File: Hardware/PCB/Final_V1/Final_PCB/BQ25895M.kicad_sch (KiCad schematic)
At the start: 17 parts, among them IC1 BQ25895MRTWT

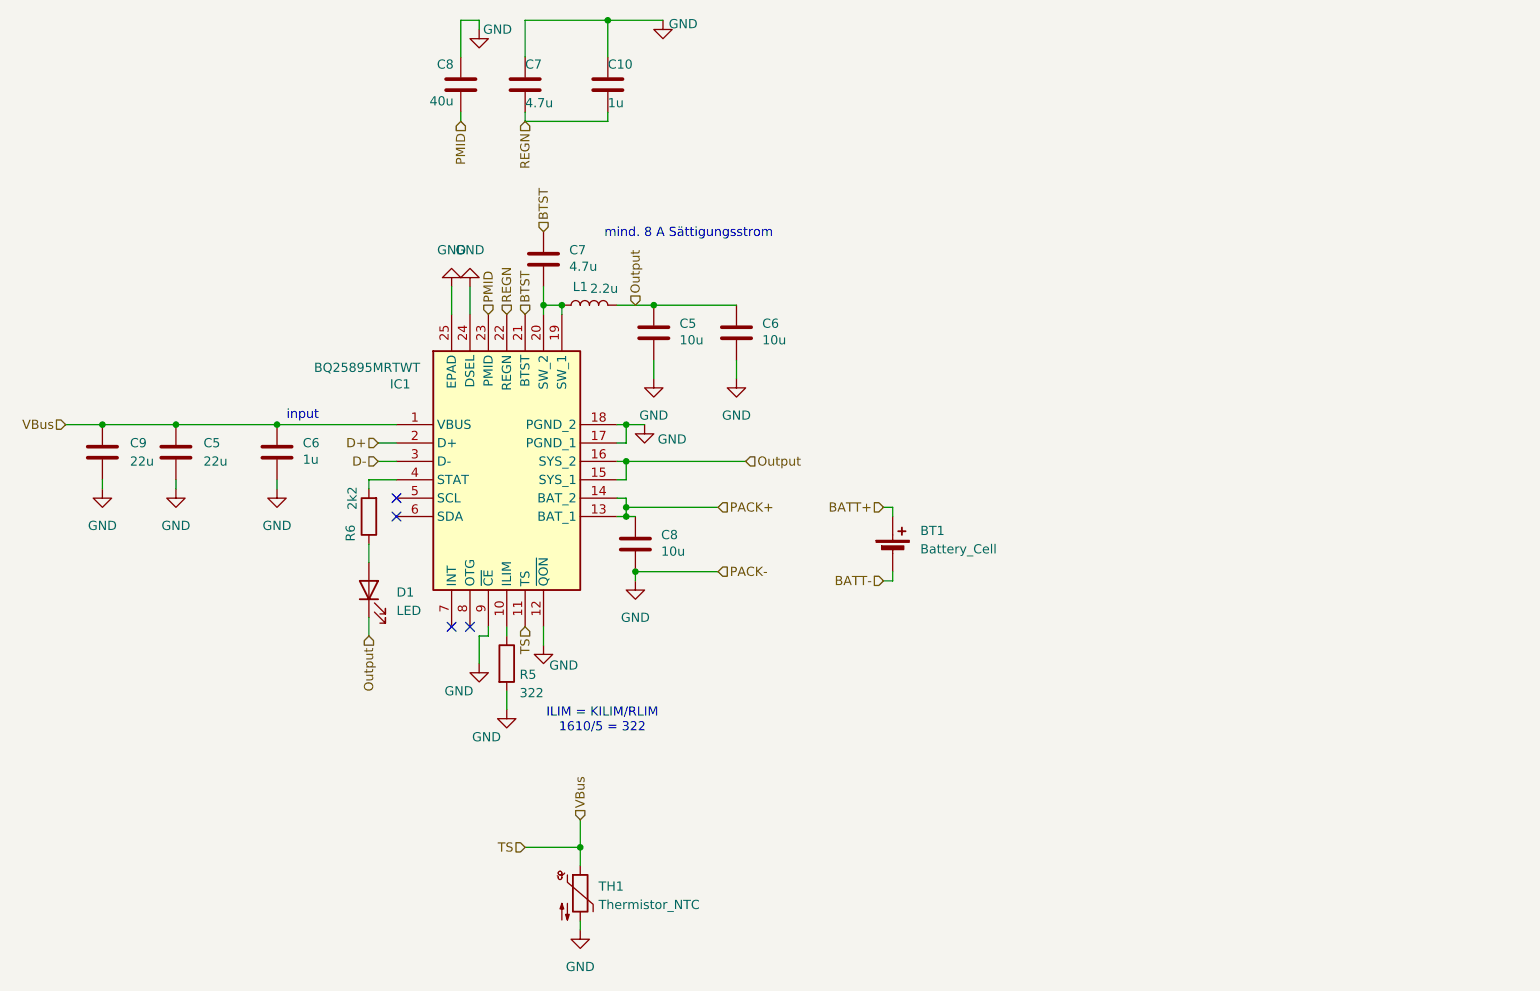
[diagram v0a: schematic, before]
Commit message: added Voltage regulator to get constant 3.3V Voltage and fixed some issues
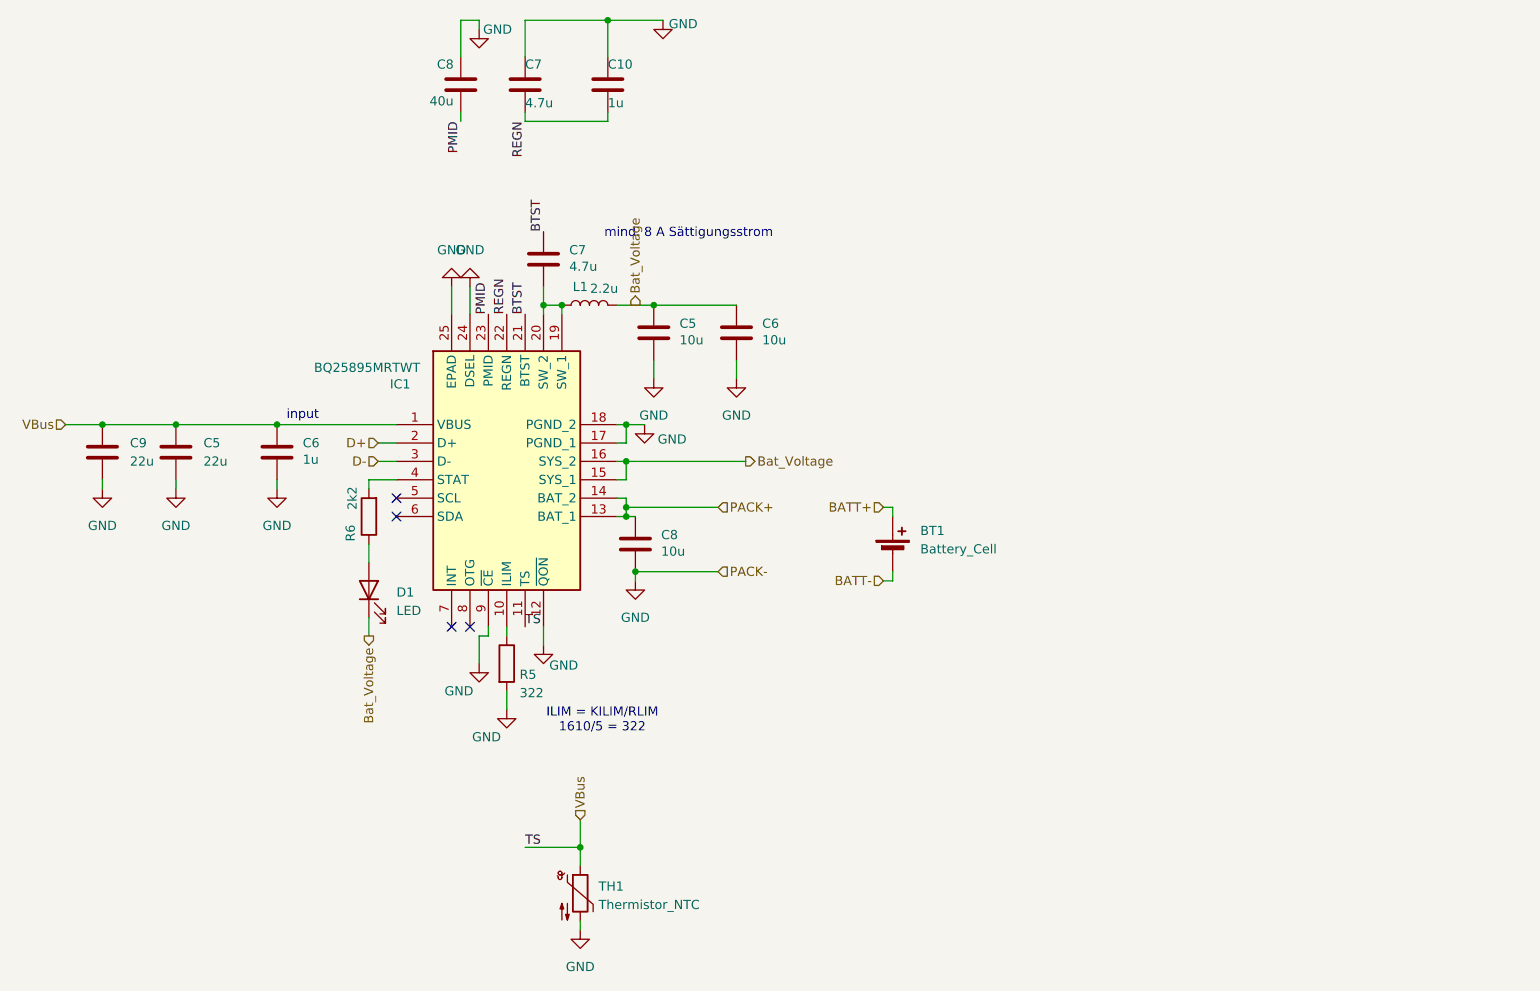
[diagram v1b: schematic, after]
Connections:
- net Output renamed Bat_Voltage
- net TS renamed VBus
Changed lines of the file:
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@@
+		)
+	)
+	(label "BTST"
+		(at 133.35 69.85 90)
+		(effects
+			(font
+				(size 1.27 1.27)
+			)
+			(justify left bottom)
+		)
+	)
+	(label "PMID"
+		(at 128.27 69.85 90)
+		(effects
+			(font
+				(size 1.27 1.27)
+			)
+			(justify left bottom)
+		)
+	)
+	(label "REGN"
+		(at 133.35 43.18 270)
+		(effects
+			(font
+				(size 1.27 1.27)
+			)
+			(justify right bottom)
+		)
+	)
+	(label "REGN"
+		(at 130.81 69.85 90)
+		(effects
+			(font
+				(size 1.27 1.27)
+			)
+			(justify left bottom)
+		)
+	)
+	(label "TS"
+		(at 133.35 113.03 0)
+		(effects
+			(font
+				(size 1.27 1.27)
+			)
+			(justify left bottom)
+		)
+	)
+	(label "BTST"
+		(at 135.89 58.42 90)
+		(effects
+			(font
+				(size 1.27 1.27)
+			)
+			(justify left bottom)
+		)
+	)
+	(label "TS"
+		(at 133.35 143.51 0)
+		(effects
+			(font
+				(size 1.27 1.27)
+			)
+			(justify left bottom)
+		)
+	)
+	(label "PMID"
+		(at 124.46 43.18 270)
+		(effects
+			(font
+				(size 1.27 1.27)
+			)
+			(justify right bottom)
 		)
 	)
@@
 		)
 	)
-	(hierarchical_label "Output"
-		(shape input)
+	(hierarchical_label "Bat_Voltage"
+		(shape output)
 		(at 163.83 90.17 0)
 		(effects
@@
 		)
 	)
-	(hierarchical_label "Output"
-		(shape input)
+	(hierarchical_label "Bat_Voltage"
+		(shape output)
 		(at 111.76 114.3 270)
 		(effects
@@
 		)
 	)
-	(hierarchical_label "PMID"
-		(shape input)
-		(at 128.27 69.85 90)
-		(effects
-			(font
-				(size 1.27 1.27)
-			)
-			(justify left)
-		)
-	)
 	(hierarchical_label "BATT+"
 		(shape input)
@@
 		)
 	)
-	(hierarchical_label "REGN"
-		(shape input)
-		(at 130.81 69.85 90)
-		(effects
-			(font
-				(size 1.27 1.27)
-			)
-			(justify left)
-		)
-	)
-	(hierarchical_label "Output"
-		(shape input)
+	(hierarchical_label "Bat_Voltage"
+		(shape output)
 		(at 148.59 68.58 90)
 		(effects
@@
 		)
 	)
-	(hierarchical_label "BTST"
-		(shape input)
-		(at 135.89 58.42 90)
-		(effects
-			(font
-				(size 1.27 1.27)
-			)
-			(justify left)
-		)
-	)
 	(hierarchical_label "PACK-"
 		(shape input)
@@
 		)
 	)
-	(hierarchical_label "PMID"
-		(shape input)
-		(at 124.46 43.18 270)
-		(effects
-			(font
-				(size 1.27 1.27)
-			)
-			(justify right)
-		)
-	)
 	(hierarchical_label "PACK+"
 		(shape input)
@@
 		(effects
 			(font
-				(size 1.27 1.27)
-			)
-			(justify left)
-		)
-	)
-	(hierarchical_label "TS"
-		(shape input)
-		(at 133.35 113.03 270)
-		(effects
-			(font
-				(size 1.27 1.27)
-			)
-			(justify right)
-		)
-	)
-	(hierarchical_label "TS"
-		(shape input)
-		(at 133.35 143.51 180)
-		(effects
-			(font
-				(size 1.27 1.27)
-			)
-			(justify right)
-		)
-	)
-	(hierarchical_label "REGN"
-		(shape input)
-		(at 133.35 43.18 270)
-		(effects
-			(font
-				(size 1.27 1.27)
-			)
-			(justify right)
-		)
-	)
-	(hierarchical_label "BTST"
-		(shape input)
-		(at 133.35 69.85 90)
-		(effects
-			(font

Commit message: fixing xhematics
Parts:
- renumbered C7 to C13, C5 to C15, C6 to C16, C8 to C17, L1 to L11
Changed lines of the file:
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@@
 		(on_board yes)
 		(dnp no)
-		(property "Reference" "#PWR013"
+		(property "Reference" "#PWR0105"
 			(at 135.89 121.92 0)
 			(effects
@@
 			(project "Final_PCB"
 				(path "/3cedac76-cdf6-4427-9720-a412bd9af7e2/3d452921-030a-4adf-89b1-90a9f65ccd40"
-					(reference "#PWR013")
+					(reference "#PWR0105")
 					(unit 1)
 				)
@@
 		(on_board yes)
 		(dnp no)
-		(property "Reference" "C5"
+		(property "Reference" "C15"
 			(at 154.686 71.12 0)
 			(effects
@@
 			(project "Final_PCB"
 				(path "/3cedac76-cdf6-4427-9720-a412bd9af7e2/3d452921-030a-4adf-89b1-90a9f65ccd40"
-					(reference "C5")
+					(reference "C15")
 					(unit 1)
 				)
@@
 		(on_board yes)
 		(dnp no)
-		(property "Reference" "C7"
+		(property "Reference" "C13"
 			(at 133.35 35.306 0)
 			(effects
@@
 			(project "Final_PCB"
 				(path "/3cedac76-cdf6-4427-9720-a412bd9af7e2/3d452921-030a-4adf-89b1-90a9f65ccd40"
-					(reference "C7")
+					(reference "C13")
 					(unit 1)
 				)
@@
 		(dnp no)
 		(fields_autoplaced yes)
-		(property "Reference" "#PWR014"
+		(property "Reference" "#PWR0106"
 			(at 140.97 161.29 0)
 			(effects
@@
 			(project "Final_PCB"
 				(path "/3cedac76-cdf6-4427-9720-a412bd9af7e2/3d452921-030a-4adf-89b1-90a9f65ccd40"
-					(reference "#PWR014")
+					(reference "#PWR0106")
 					(unit 1)
 				)
@@
 		(on_board yes)
 		(dnp no)
-		(property "Reference" "C6"
+		(property "Reference" "C16"
 			(at 166.116 71.12 0)
 			(effects
@@
 			(project "Final_PCB"
 				(path "/3cedac76-cdf6-4427-9720-a412bd9af7e2/3d452921-030a-4adf-89b1-90a9f65ccd40"
-					(reference "C6")
+					(reference "C16")
 					(unit 1)
 				)
@@
 		(dnp no)
 		(fields_autoplaced yes)
-		(property "Reference" "#PWR018"
+		(property "Reference" "#PWR0109"
 			(at 74.93 100.33 0)
 			(effects
@@
 			(project "Final_PCB"
 				(path "/3cedac76-cdf6-4427-9720-a412bd9af7e2/3d452921-030a-4adf-89b1-90a9f65ccd40"
-					(reference "#PWR018")
+					(reference "#PWR0109")
 					(unit 1)
 				)
@@
 		(on_board yes)
 		(dnp no)
-		(property "Reference" "#PWR012"
+		(property "Reference" "#PWR0104"
 			(at 130.81 130.81 0)
 			(effects
@@
 			(project "Final_PCB"
 				(path "/3cedac76-cdf6-4427-9720-a412bd9af7e2/3d452921-030a-4adf-89b1-90a9f65ccd40"
-					(reference "#PWR012")
+					(reference "#PWR0104")
 					(unit 1)
 				)
@@
 		(dnp no)
 		(fields_autoplaced yes)
-		(property "Reference" "#PWR010"
+		(property "Reference" "#PWR0108"
 			(at 99.06 100.33 0)
 			(effects
@@
 			(project "Final_PCB"
 				(path "/3cedac76-cdf6-4427-9720-a412bd9af7e2/3d452921-030a-4adf-89b1-90a9f65ccd40"
-					(reference "#PWR010")
+					(reference "#PWR0108")
 					(unit 1)
 				)
@@
 		(on_board yes)
 		(dnp no)
-		(property "Reference" "L1"
+		(property "Reference" "L11"
 			(at 140.97 66.04 90)
 			(effects
@@
 			(project "Final_PCB"
 				(path "/3cedac76-cdf6-4427-9720-a412bd9af7e2/3d452921-030a-4adf-89b1-90a9f65ccd40"
-					(reference "L1")
+					(reference "L11")
 					(unit 1)
 				)
@@
 		(on_board yes)
 		(dnp no)
-		(property "Reference" "C8"
+		(property "Reference" "C17"
 			(at 121.158 35.306 0)
 			(effects
@@
 			(project "Final_PCB"
 				(path "/3cedac76-cdf6-4427-9720-a412bd9af7e2/3d452921-030a-4adf-89b1-90a9f65ccd40"
-					(reference "C8")
+					(reference "C17")
 					(unit 1)
 				)
@@
 		(dnp no)
 		(fields_autoplaced yes)
-		(property "Reference" "#PWR09"
+		(property "Reference" "#PWR0107"
 			(at 85.09 100.33 0)
 			(effects
@@
 			(project "Final_PCB"
 				(path "/3cedac76-cdf6-4427-9720-a412bd9af7e2/3d452921-030a-4adf-89b1-90a9f65ccd40"
-					(reference "#PWR09")
+					(reference "#PWR0107")
 					(unit 1)
 				)
@@
 		(on_board yes)
 		(dnp no)
-		(property "Reference" "#PWR011"
+		(property "Reference" "#PWR0110"
 			(at 127 124.46 0)
 			(effects
@@
 			(project "Final_PCB"
 				(path "/3cedac76-cdf6-4427-9720-a412bd9af7e2/3d452921-030a-4adf-89b1-90a9f65ccd40"
-					(reference "#PWR011")
-					(unit 1)
-				)
+					(reference "#PWR0110")
+					(unit 1)
+				)

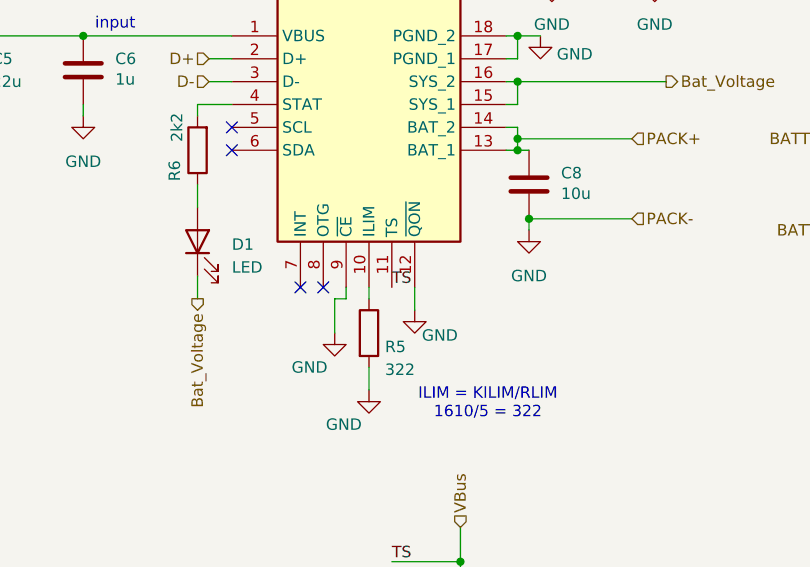
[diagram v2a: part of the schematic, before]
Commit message: #1: Add footprints to the components
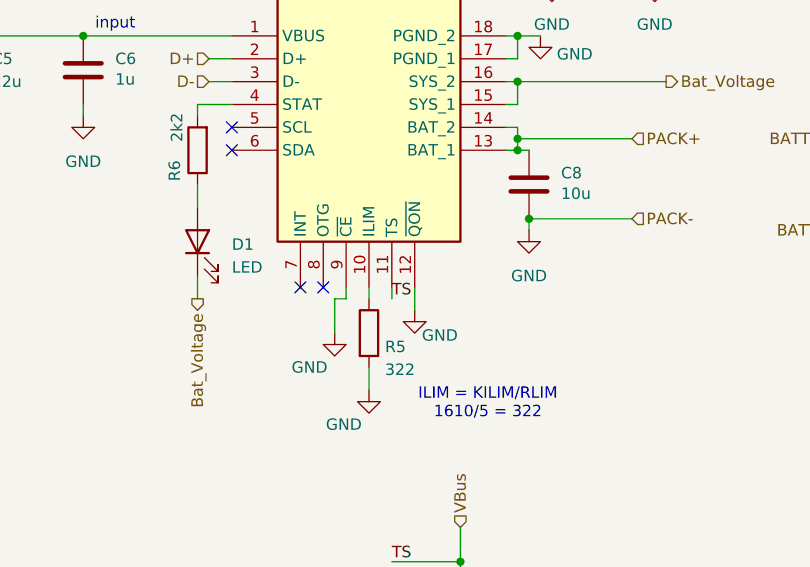
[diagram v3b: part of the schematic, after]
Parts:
- IC1: footprint QFN50P400X400X80-25N-D -> custom:QFN50P400X400X80-25N-D
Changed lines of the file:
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@@
+	(wire
+		(pts
+			(xy 133.35 114.3) (xy 133.35 113.03)
+		)
+		(stroke
+			(width 0)
+			(type default)
+		)
+	)
 	(wire
 		(pts
@@
 	)
 	(label "TS"
-		(at 133.35 113.03 0)
+		(at 133.35 114.3 0)
 		(effects
 			(font
@@
 			)
 		)
-		(property "Footprint" "QFN50P400X400X80-25N-D"
+		(property "Footprint" "custom:QFN50P400X400X80-25N-D"
 			(at 142.24 172.39 0)
 			(effects

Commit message: reapplied fixes because of commiting problems
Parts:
- removed C10: 1u, Capacitor_SMD:C_0603_1608Metric, symbol Device:C
- removed C5, C9: 22u, Capacitor_SMD:C_0603_1608Metric, symbol Device:C
- removed TH1: Thermistor_NTC, Resistor_SMD:R_0603_1608Metric, symbol Device:Thermistor_NTC
- added R11, R12, R15, R16, R17, R18, R4: 10k, Resistor_SMD:R_0603_1608Metric, symbol Device:R
- C7: value 4.7u -> 47u
- R5: value 322 -> 260
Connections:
- net GND: now also R18.1, R4.2; no longer IC1.12 (~{QON}), IC1.9 (~{CE})
- net REGN: now also R11.1
- net VBus: now also R12.2, R15.2, R16.2, R17.2; no longer IC1.11 (TS)
- net SCL: now reaches IC1.5 (SCL)
- net SCL: now also R15.1
- net SDA: now reaches IC1.6 (SDA)
- net SDA: now also R12.1
- net INT: now reaches IC1.7 (INT)
- net INT: now also R16.1
- net OTG: now reaches IC1.8 (OTG)
- net OTG: now also R17.1
- new net: IC1.9 (~{CE}), R18.2
- new net TS: IC1.11 (TS), R11.2, R4.1
- no-connect marks 4 -> 1
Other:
- moved on the sheet: D1, R6
